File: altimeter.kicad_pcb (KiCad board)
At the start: 4 copper layers, 12 x 34 mm, 39 parts, among them J1 USB_C_Receptacle_USB2.0_16P, J3 TagConnect, SW2 SW_SPDT, U1 nRF52833_QDxx, U2 MCP73832, U3 BMP390L, U4 W25X40CLUXIG, U5 LIS2DH, Y1 Crystal_GND24

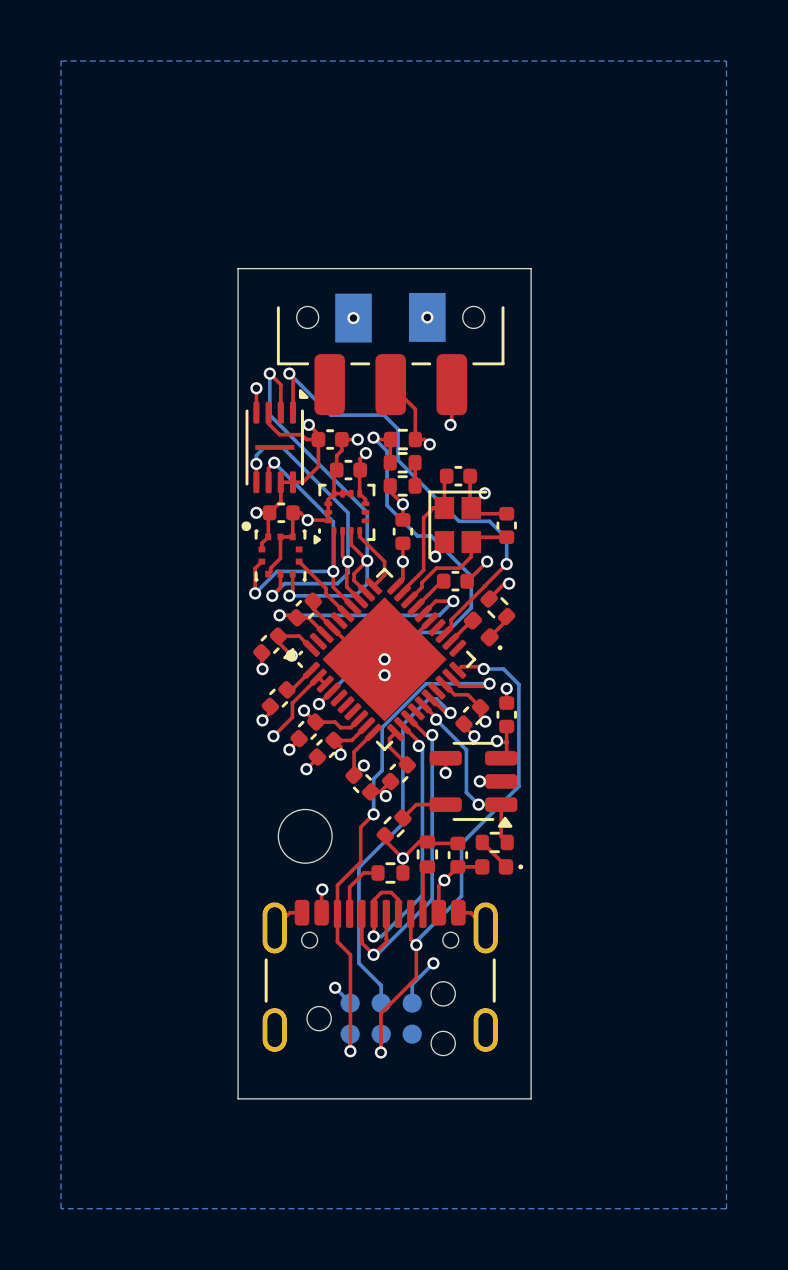
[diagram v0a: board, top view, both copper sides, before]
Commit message: add LCSC BOM
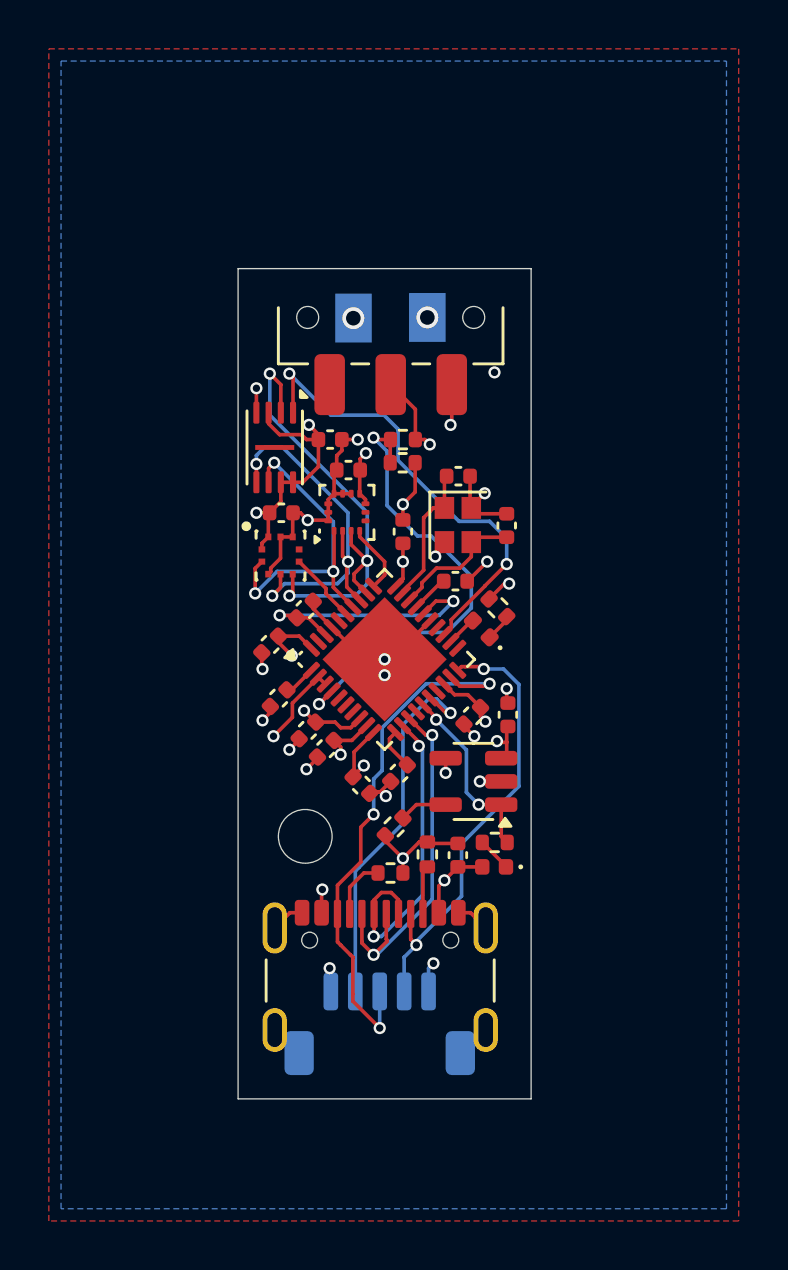
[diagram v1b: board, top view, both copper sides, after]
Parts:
- removed J3: TagConnect, Connector:Tag-Connect_TC2030-IDC-NL_2x03_P1.27mm_Vertical
- removed R4: 5.1k, Resistor_SMD:R_0402_1005Metric
- added G***: LOGO, LOGO, B.Cu at (222.5, 89.8)
- added J2: Conn_01x05_MountingPin, Connector_JST:JST_SH_BM05B-SRSS-TB_1x05-1MP_P1.00mm_Vertical, B.Cu at (219.8, 97.9)
- R2: value 30k -> 100k
- R5: value 5.1k -> 51k
- R8: value 30k -> 51k
- U2: value MCP73832 -> MCP73832T-2
- Y1: value Crystal_GND24 -> 32MHz
- moved C13 0.07 mm to (219.1, 88.2)
- moved C17 0.05 mm to (225.1, 85.3)
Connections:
- R5 pad 2: Net-(R4-Pad1) -> Earth
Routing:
- net /SWCLK: track 22.4 -> 18.8 mm, vias 3 -> 2
- net Net-(R4-Pad1): track 0.95 -> 0.00 mm
- net NRF_VDD: track 43.5 -> 42.7 mm
- net /NRST: track 16.2 -> 15.4 mm
- net +1V8: vias 4 -> 5
- added copper zone on F.Cu, net Earth

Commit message: ordered version
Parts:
- C15, C16: value 12pF -> 12p
- C6: value 0.1u -> 100p
- moved C1 164.5 mm to (62.1, 54.1)
- moved C10 164.5 mm to (55.3, 54.7)
- moved C11 164.5 mm to (59.2, 46.5)
- moved C12 164.5 mm to (56.1, 55.4)
- moved C13 164.5 mm to (57.5, 56.9)
- moved C14 164.5 mm to (55.2, 49.7)
- moved C15 164.5 mm to (63.5, 46.3)
- moved C16 164.5 mm to (61.5, 44.2)
- moved C17 164.5 mm to (63.5, 54.0)
- moved C18 164.5 mm to (56.3, 42.8)
- moved C2 164.5 mm to (61.5, 59.8)
- moved C3 164.5 mm to (57.0, 44.0)
- moved C4 164.5 mm to (54.3, 45.8)
- moved C5 164.5 mm to (53.8, 51.1)
- moved C6 164.5 mm to (61.4, 48.5)
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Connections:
- J1 pad A6: /D_N -> /D_P
- J1 pad A7: /D_P -> /D_N
- J1 pad B6: /D_N -> /D_P
- J1 pad B7: /D_P -> /D_N
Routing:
- net +1V8: track 15.9 -> 24.2 mm
- net /D_N: track 13.3 -> 14.8 mm
- net /VSENSE: track 19.3 -> 20.5 mm
- net /D_P: track 15.1 -> 13.9 mm
- net Earth: vias 21 -> 23

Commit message: actually ordered version
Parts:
- moved U5 0.38 mm to (57.1, 46.1), turned to 135 degrees
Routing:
- net Earth: track 42.1 -> 39.7 mm, vias 23 -> 24
